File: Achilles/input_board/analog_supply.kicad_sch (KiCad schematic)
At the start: 26 parts, among them IC1 LM5157RTER, U2 TPS7A4701xRGW, U3 INA290A3

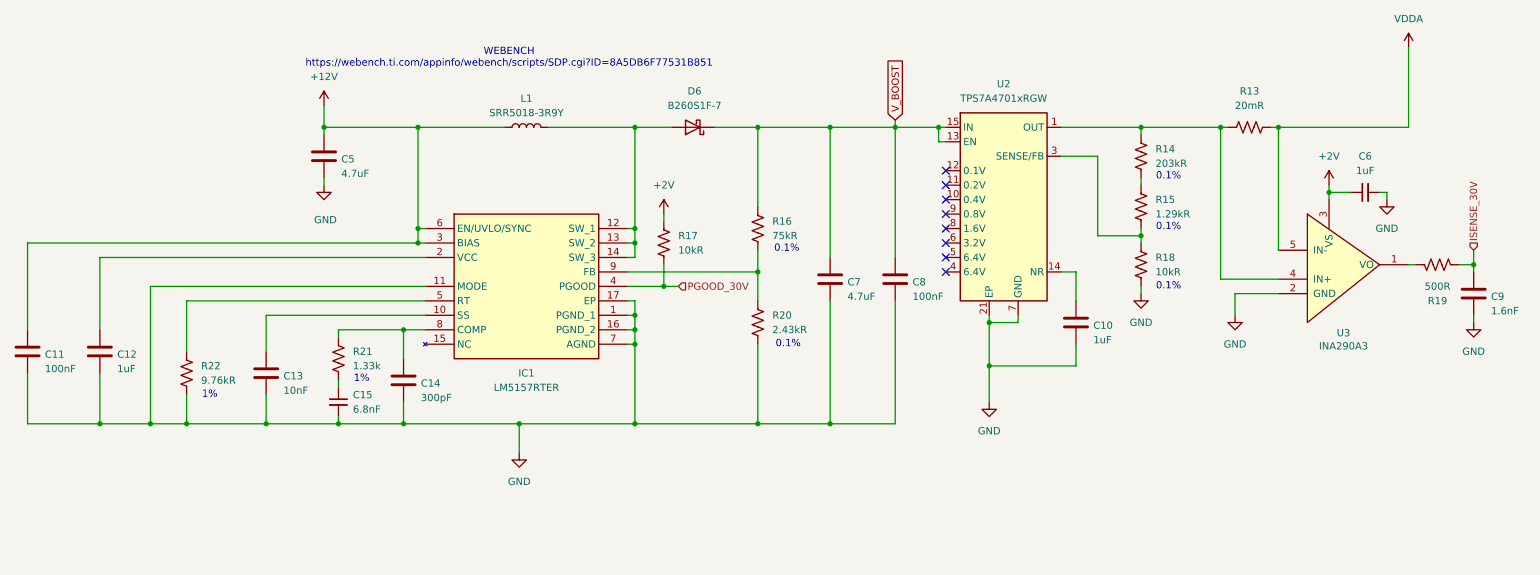
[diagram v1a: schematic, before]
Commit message: Resize boost caps in sim; update pcb with PNs
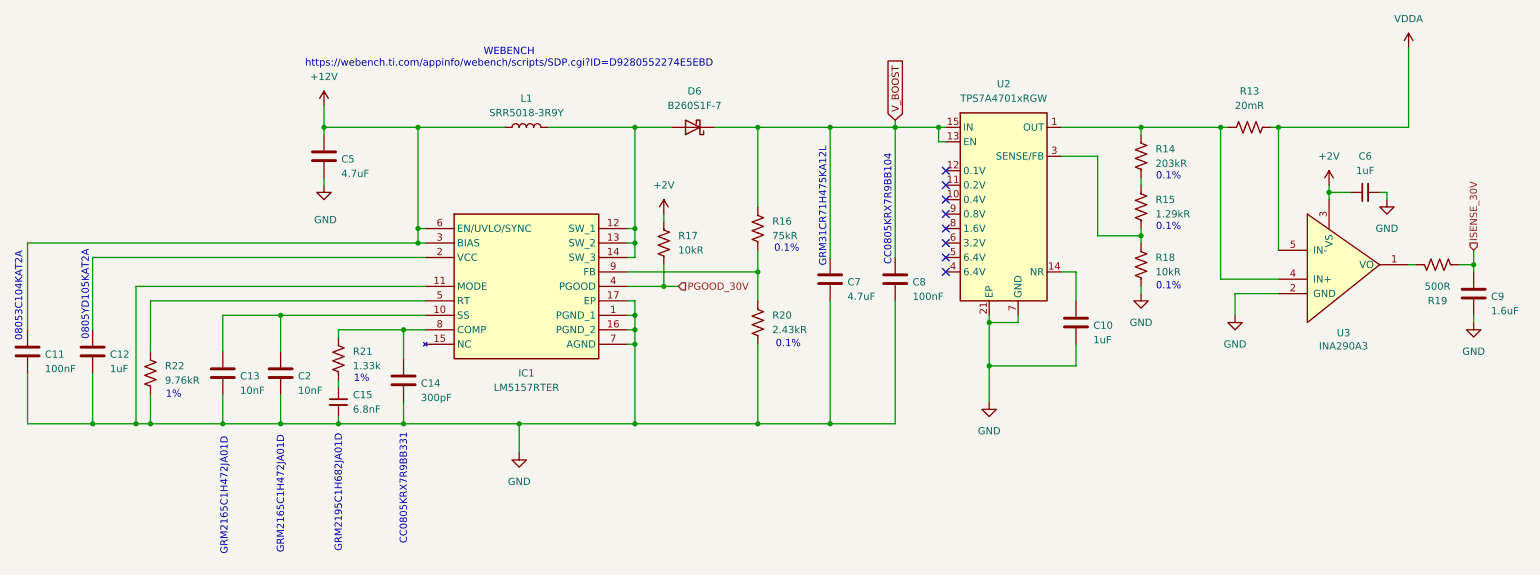
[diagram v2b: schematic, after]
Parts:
- added C2: 10nF, Capacitor_SMD:C_0805_2012Metric_Pad1.18x1.45mm_HandSolder, symbol Device:C
- C7: footprint Capacitor_SMD:C_0805_2012Metric_Pad1.18x1.45mm_HandSolder -> Capacitor_SMD:C_1206_3216Metric_Pad1.33x1.80mm_HandSolder
- C9: value 1.6nF -> 1.6uF
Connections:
- net GND: now also C2.2
- net at C13.1, IC1.10 (SS): now also C2.1
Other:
- note added: "08053C104KAT2A"
- note added: "0805YD105KAT2A"
- note added: "CC0805KRX7R9BB104"
- note added: "CC0805KRX7R9BB331"
- note added: "GRM2165C1H472JA01D"
- note added: "GRM2195C1H682JA01D"
- note added: "GRM31CR71H475KA12L"
- note added: "WEBENCH https://webench.ti.com/appinfo/webench/scripts/SDP.cgi?ID=D9280552274E5EBD"
- note removed: "WEBENCH https://webench.ti.com/appinfo/webench/scripts/SDP.cgi?ID=8A5DB6F77531B851"
- moved on the sheet: C12, C13, R22
